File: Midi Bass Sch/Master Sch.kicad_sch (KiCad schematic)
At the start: 13 parts, among them J1 DIN-5, U1 PIC16F1788

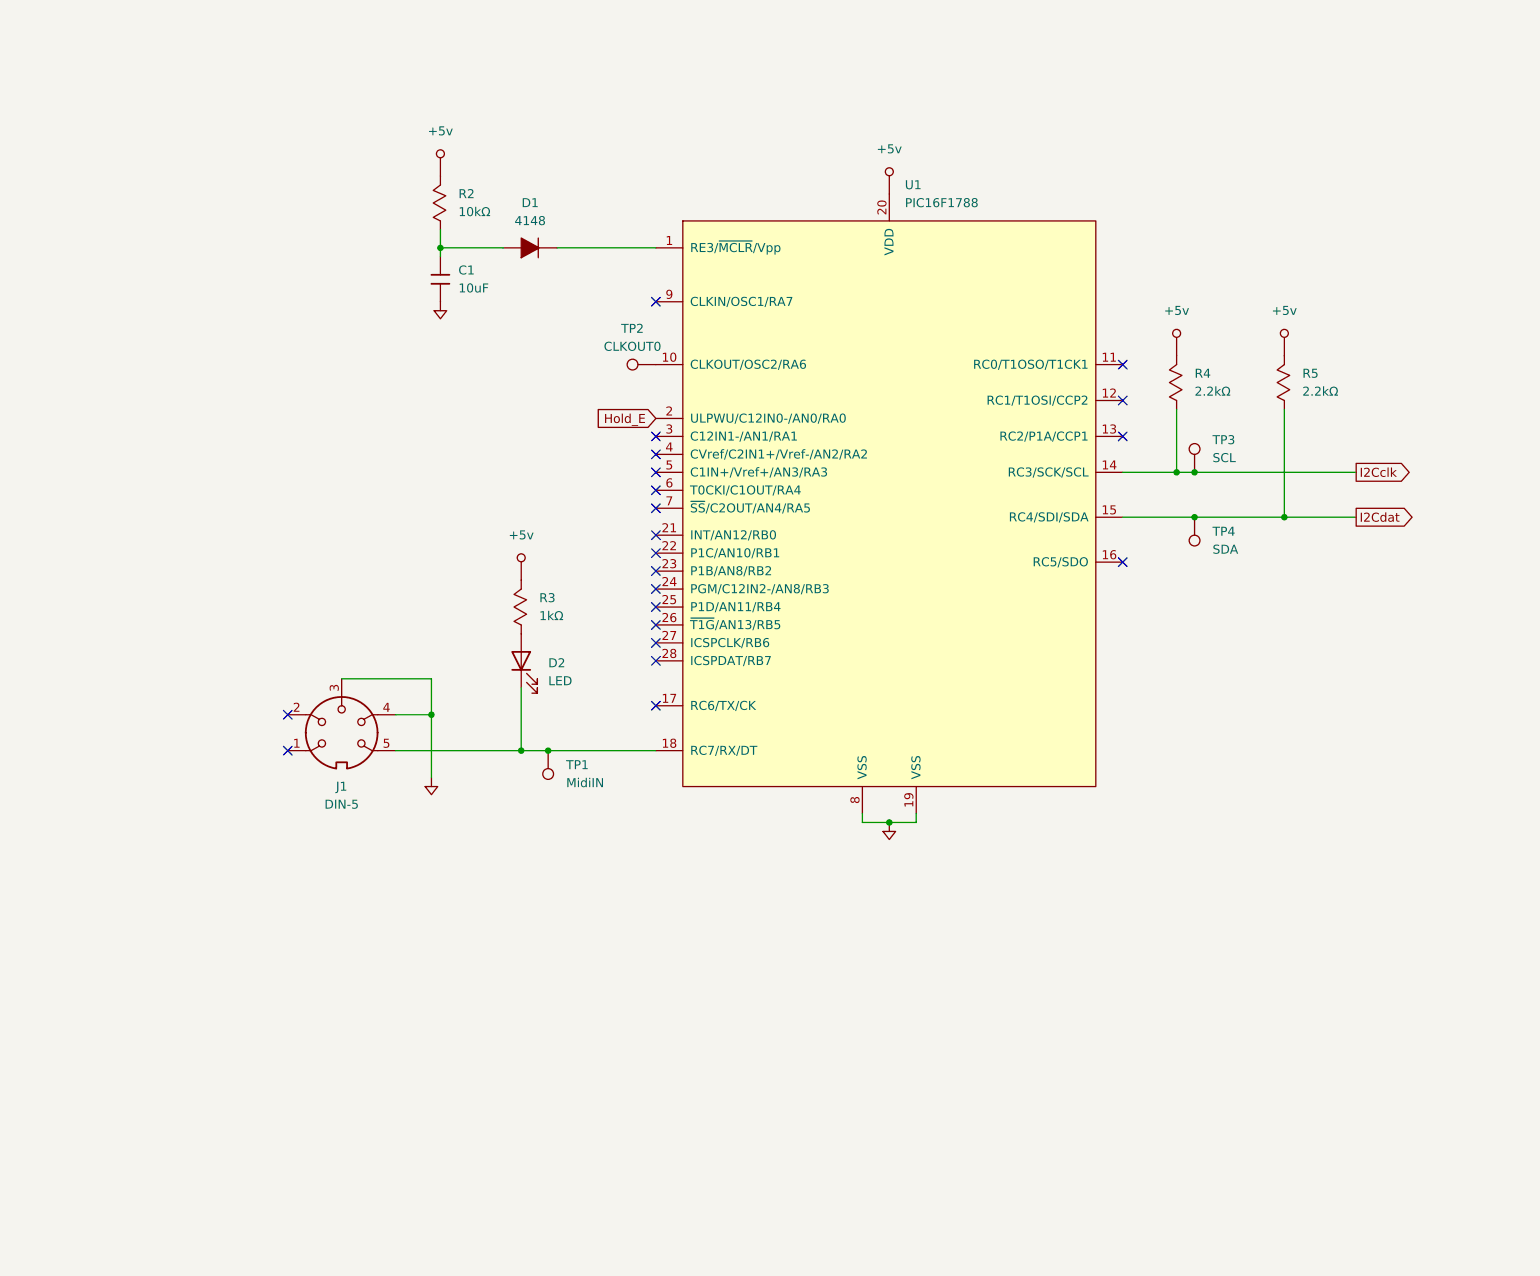
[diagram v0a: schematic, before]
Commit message: updated master schematic and block diagram updated hours as well added block diagram to report
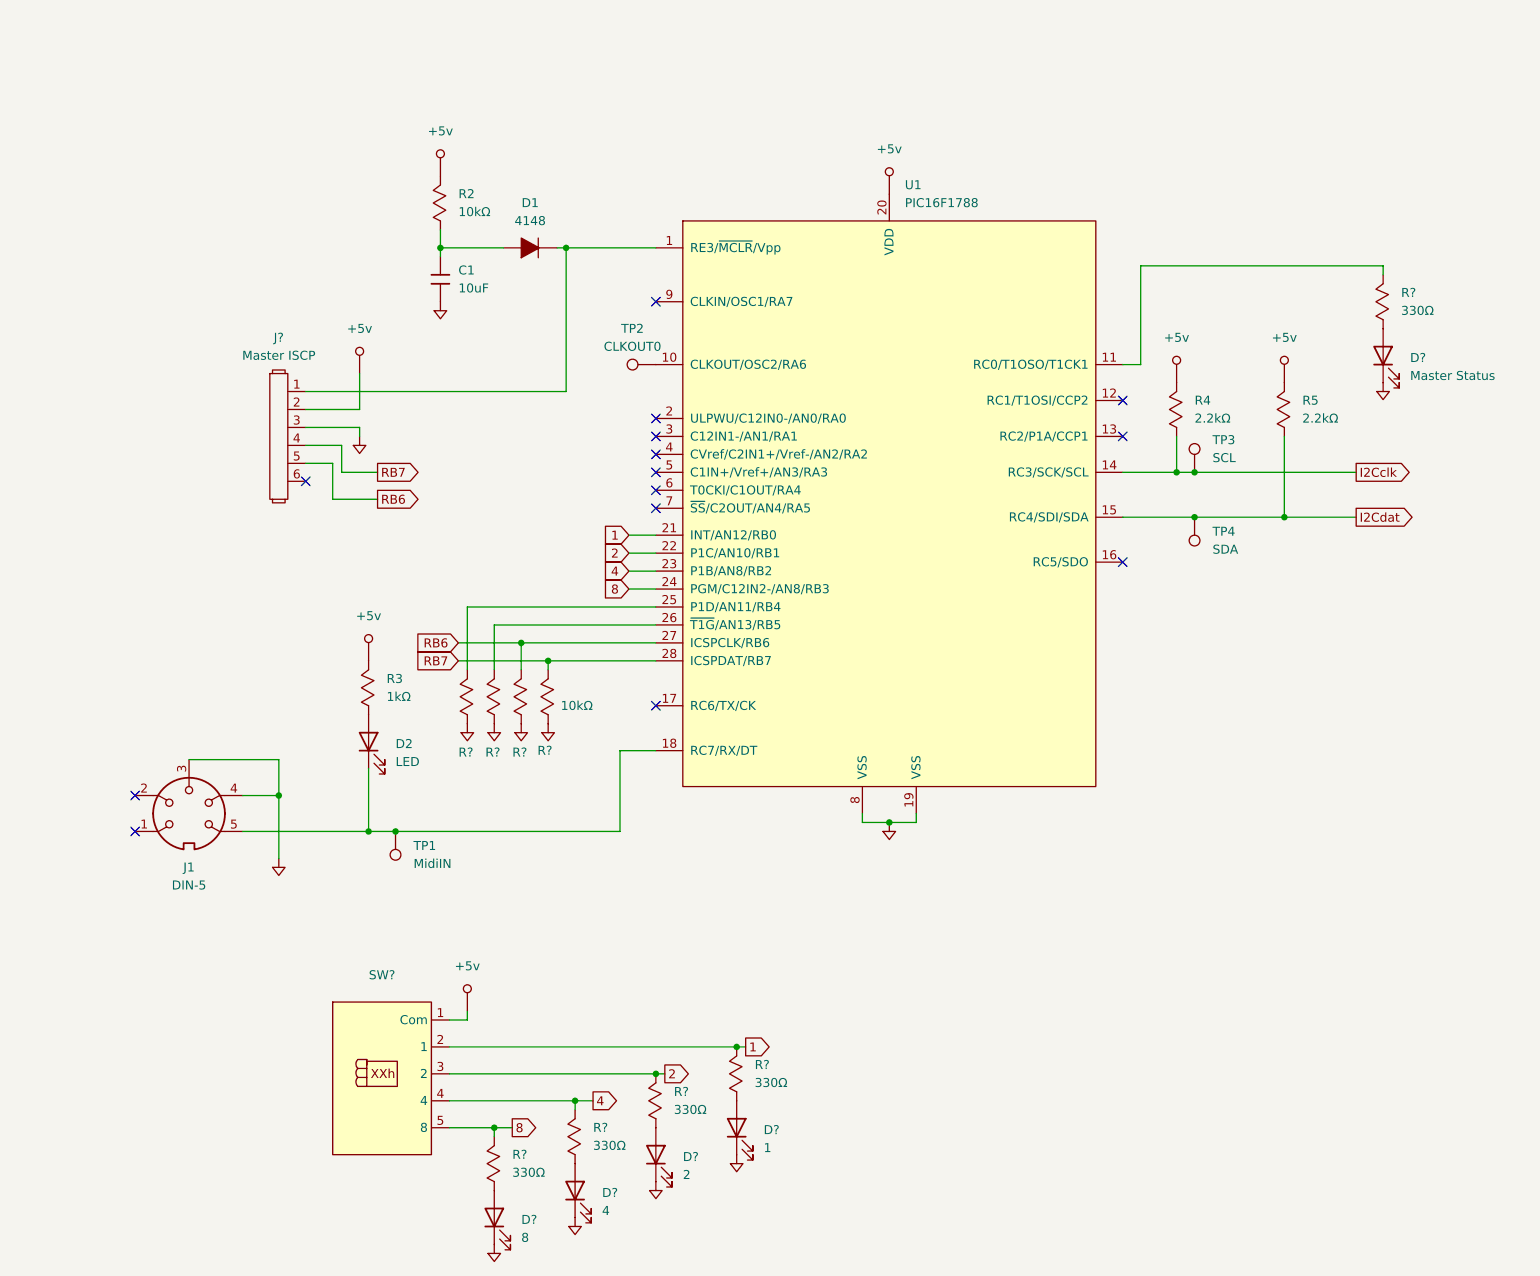
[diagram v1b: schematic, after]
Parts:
- added D?: Master Status, symbol Device:LED
- added D?: 2, symbol Device:LED
- added D?: 8, symbol Device:LED
- added D?: 1, symbol Device:LED
- added D?: 4, symbol Device:LED
- added J?: Master ISCP, symbol Owen's Symbols:Header_1x6
- added R? (x4): 10kΩ, symbol Owen's Symbols:Resistor_Mod
- added R? (x5): 330Ω, symbol Owen's Symbols:Resistor_Mod
- added SW?: ~, symbol Owen's Symbols:Hex_Rotary_Switch
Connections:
- net +5v: now also J?.2, SW?.1 (Com)
- net GND: now also D?.1 (K), D?.1 (K), D?.1 (K), D?.1 (K), D?.1 (K), J?.3, R?.1, R?.1, R?.1, R?.1
- net at D1.2, U1.1 (RE3/~{MCLR}/Vpp): now also J?.1
- net 1: now reaches U1.18 (RC7/RX/DT)
- net 1: now also R?.2, SW?.2 (1)
- new net: D?.2 (A), R?.1 (x5)
- new net 2: R?.2, SW?.3 (2)
- new net 4: R?.2, SW?.4
- new net 8: R?.2, SW?.5 (8)
- new net RB6: J?.5, R?.2
- new net RB7: J?.4, R?.2
- no-connect marks 21 -> 14
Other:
- moved on the sheet: D2, J1, R3, R4, R5, TP1

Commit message: updated slave to 1789 to reflect new design updated 1789 to reflect thin flat pack
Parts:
- gave numbers to parts that had none: 16
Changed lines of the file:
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@@
 		(dnp no)
 		(fields_autoplaced yes)
-		(property "Reference" "SW?"
+		(property "Reference" "SW2"
 			(at 75.565 149.86 0)
 			(effects
@@
 			(project ""
 				(path "/06818073-fb22-48ee-acc5-6dedd827034e/0dc3b915-e001-48bd-b9bb-7010249087fd"
-					(reference "SW?")
+					(reference "SW2")
 					(unit 1)
 				)
@@
 		(on_board yes)
 		(dnp no)
-		(property "Reference" "R?"
+		(property "Reference" "R22"
 			(at 86.36 118.364 90)
 			(effects
@@
 			(project "Midi Bass Sch"
 				(path "/06818073-fb22-48ee-acc5-6dedd827034e/0dc3b915-e001-48bd-b9bb-7010249087fd"
-					(reference "R?")
+					(reference "R22")
 					(unit 1)
 				)
@@
 		(dnp no)
 		(fields_autoplaced yes)
-		(property "Reference" "R?"
+		(property "Reference" "R24"
 			(at 93.98 175.2599 90)
 			(effects
@@
 			(project "Midi Bass Sch"
 				(path "/06818073-fb22-48ee-acc5-6dedd827034e/0dc3b915-e001-48bd-b9bb-7010249087fd"
-					(reference "R?")
+					(reference "R24")
 					(unit 1)
 				)
@@
 		(on_board yes)
 		(dnp no)
-		(property "Reference" "R?"
+		(property "Reference" "R23"
 			(at 90.17 118.364 90)
 			(effects
@@
 			(project "Midi Bass Sch"
 				(path "/06818073-fb22-48ee-acc5-6dedd827034e/0dc3b915-e001-48bd-b9bb-7010249087fd"
-					(reference "R?")
+					(reference "R23")
 					(unit 1)
 				)
@@
 		(dnp no)
 		(fields_autoplaced yes)
-		(property "Reference" "R?"
+		(property "Reference" "R29"
 			(at 128.27 162.5599 90)
 			(effects
@@
 			(project "Midi Bass Sch"
 				(path "/06818073-fb22-48ee-acc5-6dedd827034e/0dc3b915-e001-48bd-b9bb-7010249087fd"
-					(reference "R?")
+					(reference "R29")
 					(unit 1)
 				)
@@
 		(dnp no)
 		(fields_autoplaced yes)
-		(property "Reference" "D?"
+		(property "Reference" "D14"
 			(at 220.98 62.5474 90)
 			(effects
@@
 			(project "Midi Bass Sch"
 				(path "/06818073-fb22-48ee-acc5-6dedd827034e/0dc3b915-e001-48bd-b9bb-7010249087fd"
-					(reference "D?")
+					(reference "D14")
 					(unit 1)
 				)
@@
 		(dnp no)
 		(fields_autoplaced yes)
-		(property "Reference" "D?"
+		(property "Reference" "D12"
 			(at 118.11 175.5774 90)
 			(effects
@@
 			(project "Midi Bass Sch"
 				(path "/06818073-fb22-48ee-acc5-6dedd827034e/0dc3b915-e001-48bd-b9bb-7010249087fd"
-					(reference "D?")
+					(reference "D12")
 					(unit 1)
 				)
@@
 		(on_board yes)
 		(dnp no)
-		(property "Reference" "R?"
+		(property "Reference" "R26"
 			(at 97.536 118.11 90)
 			(effects
@@
 			(project ""
 				(path "/06818073-fb22-48ee-acc5-6dedd827034e/0dc3b915-e001-48bd-b9bb-7010249087fd"
-					(reference "R?")
+					(reference "R26")
 					(unit 1)
 				)
@@
 		(dnp no)
 		(fields_autoplaced yes)
-		(property "Reference" "R?"
+		(property "Reference" "R28"
 			(at 116.84 166.3699 90)
 			(effects
@@
 			(project "Midi Bass Sch"
 				(path "/06818073-fb22-48ee-acc5-6dedd827034e/0dc3b915-e001-48bd-b9bb-7010249087fd"
-					(reference "R?")
+					(reference "R28")
 					(unit 1)
 				)
@@
 		(dnp no)
 		(fields_autoplaced yes)
-		(property "Reference" "D?"
+		(property "Reference" "D10"
 			(at 95.25 184.4674 90)
 			(effects
@@
 			(project "Midi Bass Sch"
 				(path "/06818073-fb22-48ee-acc5-6dedd827034e/0dc3b915-e001-48bd-b9bb-7010249087fd"
-					(reference "D?")
+					(reference "D10")
 					(unit 1)
 				)
@@
 		(dnp no)
 		(fields_autoplaced yes)
-		(property "Reference" "D?"
+		(property "Reference" "D13"
 			(at 129.54 171.7674 90)
 			(effects
@@
 			(project "Midi Bass Sch"
 				(path "/06818073-fb22-48ee-acc5-6dedd827034e/0dc3b915-e001-48bd-b9bb-7010249087fd"
-					(reference "D?")
+					(reference "D13")
 					(unit 1)
 				)
@@
 		(dnp no)
 		(fields_autoplaced yes)
-		(property "Reference" "R?"
+		(property "Reference" "R27"
 			(at 105.41 171.4499 90)
 			(effects
@@
 			(project "Midi Bass Sch"
 				(path "/06818073-fb22-48ee-acc5-6dedd827034e/0dc3b915-e001-48bd-b9bb-7010249087fd"
-					(reference "R?")
+					(reference "R27")
 					(unit 1)
 				)
@@
 		(dnp no)
 		(fields_autoplaced yes)
-		(property "Reference" "R?"
+		(property "Reference" "R30"
 			(at 219.71 53.3399 90)
 			(effects
@@
 			(project "Midi Bass Sch"
 				(path "/06818073-fb22-48ee-acc5-6dedd827034e/0dc3b915-e001-48bd-b9bb-7010249087fd"
-					(reference "R?")
+					(reference "R30")
 					(unit 1)
 				)
@@
 		(dnp no)
 		(fields_autoplaced yes)
-		(property "Reference" "D?"
+		(property "Reference" "D11"
 			(at 106.68 180.6574 90)
 			(effects
@@
 			(project "Midi Bass Sch"
 				(path "/06818073-fb22-48ee-acc5-6dedd827034e/0dc3b915-e001-48bd-b9bb-7010249087fd"
-					(reference "D?")
+					(reference "D11")
 					(unit 1)
 				)
@@
 		(on_board yes)
 		(dnp no)
-		(property "Reference" "R?"
+		(property "Reference" "R25"
 			(at 93.98 118.364 90)
 			(effects
@@
 			(project "Midi Bass Sch"
 				(path "/06818073-fb22-48ee-acc5-6dedd827034e/0dc3b915-e001-48bd-b9bb-7010249087fd"
-					(reference "R?")
+					(reference "R25")
 					(unit 1)
 				)
@@
 		(dnp no)
 		(fields_autoplaced yes)
-		(property "Reference" "J?"
+		(property "Reference" "J2"
 			(at 60.96 59.69 0)
 			(effects
@@
 			(project ""
 				(path "/06818073-fb22-48ee-acc5-6dedd827034e/0dc3b915-e001-48bd-b9bb-7010249087fd"
-					(reference "J?")
+					(reference "J2")
 					(unit 1)
 				)

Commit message: added flags to E-slave
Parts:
- TP2: value CLKOUT0 -> Master CLKOUT
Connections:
- net at TP2.1: now also U1.4 (CVref/C2IN1+/Vref-/AN2/RA2)
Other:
- moved on the sheet: TP2
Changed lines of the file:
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@@
+	(wire
+		(pts
+			(xy 180.34 44.45) (xy 180.34 52.07)
+		)
+		(stroke
+			(width 0)
+			(type default)
+		)
+	)
 	(wire
 		(pts
@@
 	(symbol
 		(lib_id "Connector:TestPoint")
-		(at 114.3 63.5 90)
+		(at 180.34 44.45 0)
 		(unit 1)
 		(exclude_from_sim no)
@@
 		(fields_autoplaced yes)
 		(property "Reference" "TP2"
-			(at 110.998 58.42 90)
-			(effects
-				(font
-					(size 1.27 1.27)
-				)
-			)
-		)
-		(property "Value" "CLKOUT0"
-			(at 110.998 60.96 90)
-			(effects
-				(font
-					(size 1.27 1.27)
-				)
-			)
-		)
-		(property "Footprint" ""
-			(at 114.3 58.42 0)
+			(at 182.88 39.8779 0)
+			(effects
+				(font
+					(size 1.27 1.27)
+				)
+				(justify left)
+			)
+		)
+		(property "Value" "Master CLKOUT"
+			(at 182.88 42.4179 0)
+			(effects
+				(font
+					(size 1.27 1.27)
+				)
+				(justify left)
+			)
+		)
+		(property "Footprint" ""
+			(at 185.42 44.45 0)
 			(effects
 				(font
@@
 		)
 		(property "Datasheet" "~"
-			(at 114.3 58.42 0)
+			(at 185.42 44.45 0)
 			(effects
 				(font
@@
 		)
 		(property "Description" "test point"
-			(at 114.3 63.5 0)
-			(effects
-				(font
+			(at 180.34 44.45 0)
+			(effects
+				(font

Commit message: added opto isolation to plucking solenoids
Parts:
- added R?: 10Ω, symbol Owen's Symbols:Resistor_Mod
- added SW?: Master Reset, symbol Switch:SW_Push
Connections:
- net GND: now also R?.1
- net at C1.1, D1.1, R2.1: now also SW?.2
- new net: R?.2, SW?.1
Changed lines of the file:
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@@
 	)
 	(junction
+		(at 83.82 45.72)
+		(diameter 0)
+		(color 0 0 0 0)
+	)
+	(junction
 		(at 147.32 128.27)
 		(diameter 0)
@@
 	(wire
 		(pts
+			(xy 83.82 45.72) (xy 83.82 44.45)
+		)
+		(stroke
+			(width 0)
+			(type default)
+		)
+	)
+	(wire
+		(pts
 			(xy 91.44 171.45) (xy 91.44 172.72)
 		)
@@
 	(wire
 		(pts
+			(xy 80.01 45.72) (xy 83.82 45.72)
+		)
+		(stroke
+			(width 0)
+			(type default)
+		)
+	)
+	(wire
+		(pts
 			(xy 55.88 129.54) (xy 73.66 129.54)
 		)
@@
 	(wire
 		(pts
+			(xy 63.5 48.26) (xy 63.5 45.72)
+		)
+		(stroke
+			(width 0)
+			(type default)
+		)
+	)
+	(wire
+		(pts
 			(xy 102.87 167.64) (xy 105.41 167.64)
 		)
@@
 	(wire
 		(pts
-			(xy 83.82 46.99) (xy 83.82 44.45)
+			(xy 83.82 46.99) (xy 83.82 45.72)
 		)
 		(stroke
@@
 	(wire
 		(pts
+			(xy 63.5 45.72) (xy 69.85 45.72)
+		)
+		(stroke
+			(width 0)
+			(type default)
+		)
+	)
+	(wire
+		(pts
 			(xy 68.58 77.47) (xy 64.77 77.47)
 		)
@@
 	)
 	(symbol
+		(lib_id "Owen's Symbols:Resistor_Mod")
+		(at 63.5 52.07 90)
+		(unit 1)
+		(exclude_from_sim no)
+		(in_bom yes)
+		(on_board yes)
+		(dnp no)
+		(fields_autoplaced yes)
+		(property "Reference" "R?"
+			(at 66.04 50.7999 90)
+			(effects
+				(font
+					(size 1.27 1.27)
+				)
+				(justify right)
+			)
+		)
+		(property "Value" "10Ω"
+			(at 66.04 53.3399 90)
+			(effects
+				(font
+					(size 1.27 1.27)
+				)
+				(justify right)
+			)
+		)
+		(property "Footprint" ""
+			(at 60.96 53.34 0)
+			(effects
+				(font
+					(size 1.27 1.27)
+				)
+				(hide yes)
+			)
+		)
+		(property "Datasheet" ""
+			(at 60.96 53.34 0)
+			(effects
+				(font
+					(size 1.27 1.27)
+				)
+				(hide yes)
+			)
+		)
+		(property "Description" ""
+			(at 63.5 52.07 0)
+			(effects
+				(font
+					(size 1.27 1.27)
+				)
+				(hide yes)
+			)
+		)
+		(pin "2"
+		)
+		(pin "1"
+		)
+		(instances
+			(project "Midi Bass Sch"
+				(path "/06818073-fb22-48ee-acc5-6dedd827034e/0dc3b915-e001-48bd-b9bb-7010249087fd"
+					(reference "R?")
+					(unit 1)
+				)
+			)
+		)
+	)
+	(symbol
 		(lib_id "Connector:TestPoint")
 		(at 190.5 78.74 0)
@@
 	)
 	(symbol
+		(lib_id "Switch:SW_Push")
+		(at 74.93 45.72 0)
+		(unit 1)
+		(exclude_from_sim no)
+		(in_bom yes)
+		(on_board yes)
+		(dnp no)
+		(fields_autoplaced yes)
+		(property "Reference" "SW?"
+			(at 74.93 38.1 0)
+			(effects
+				(font
+					(size 1.27 1.27)
+				)
+			)
+		)
+		(property "Value" "Master Reset"
+			(at 74.93 40.64 0)
+			(effects
+				(font
+					(size 1.27 1.27)
+				)
+			)
+		)
+		(property "Footprint" ""
+			(at 74.93 40.64 0)
+			(effects
+				(font
+					(size 1.27 1.27)
+				)
+				(hide yes)
+			)
+		)
+		(property "Datasheet" "~"
+			(at 74.93 40.64 0)
+			(effects
+				(font
+					(size 1.27 1.27)
+				)
+				(hide yes)
+			)
+		)
+		(property "Description" "Push button switch, generic, two pins"
+			(at 74.93 45.72 0)
+			(effects
+				(font
+					(size 1.27 1.27)
+				)
+				(hide yes)
+			)
+		)
+		(pin "2"
+		)
+		(pin "1"
+		)
+		(instances
+			(project "Midi Bass Sch"
+				(path "/06818073-fb22-48ee-acc5-6dedd827034e/0dc3b915-e001-48bd-b9bb-7010249087fd"
+					(reference "SW?")
+					(unit 1)
+				)
+			)
+		)
+	)
+	(symbol
 		(lib_id "Custom Power:+5v")
 		(at 73.66 104.14 0)
@@
 					(unit 1)
 				)
+			)
+		)
+	)
+	(symbol
+		(lib_id "Custom Power:GND")
+		(at 63.5 55.88 0)
+		(unit 1)
+		(exclude_from_sim no)
+		(in_bom no)
+		(on_board no)
+		(dnp no)
+		(fields_autoplaced yes)
+		(property "Reference" "#PWR0120"
+			(at 63.5 54.61 0)
+			(effects
+				(font
+					(size 1.27 1.27)
+				)
+				(hide yes)
+			)
+		)
+		(property "Value" "GND"
+			(at 63.5 54.61 0)
+			(effects
+				(font
+					(size 1.27 1.27)
+				)
+				(hide yes)
+			)
+		)
+		(property "Footprint" ""
+			(at 63.5 54.61 0)
+			(effects
+				(font
+					(size 1.27 1.27)
+				)
+				(hide yes)
+			)
+		)
+		(property "Datasheet" ""
+			(at 63.5 54.61 0)
+			(effects
+				(font
+					(size 1.27 1.27)
+				)
+				(hide yes)
+			)
+		)
+		(property "Description" ""
+			(at 63.5 55.88 0)
+			(effects
+				(font
+					(size 1.27 1.27)
+				)
+				(hide yes)
+			)
+		)
+		(pin "~"
+		)
+		(instances
+			(project "Midi Bass Sch"
+				(path "/06818073-fb22-48ee-acc5-6dedd827034e/0dc3b915-e001-48bd-b9bb-7010249087fd"
+					(reference "#PWR0120")
+					(unit 1)
+				)

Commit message: working on system overview of report
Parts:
- gave numbers to parts that had none: 2
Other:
- moved on the sheet: C1, D1, D10, D11, D12, D13, D14, D2, J1, J2, R2, R22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

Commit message: added solenoid array for the A slave
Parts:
- renumbered D10 to D1, D11 to D3, D12 to D4, D1 to D5, D13 to D6, D14 to D7, R90 to R1, R26 to R10, R29 to R11, R4 to R12, R5 to R13, R30 to R14, R24 to R2, R27 to R4, R2 to R5, R22 to R6, R23 to R7, R28 to R8, R25 to R9, SW2 to SW1, SW3 to SW2
